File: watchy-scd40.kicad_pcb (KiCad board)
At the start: 2 copper layers, 10.3 x 17 mm, 12 parts, among them U1 SCD40-D-R2, U2 NJM2882F33

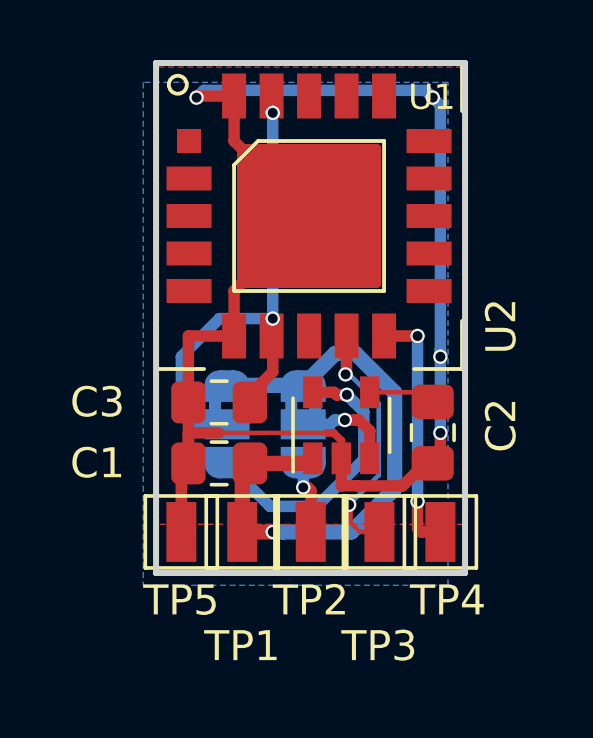
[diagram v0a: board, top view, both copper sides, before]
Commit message: v2: Tweaks to soldermask and to silkscreen
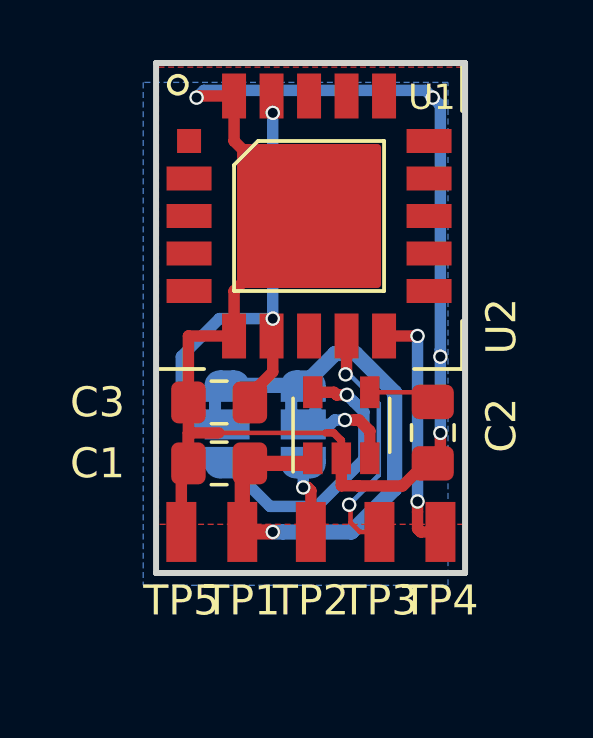
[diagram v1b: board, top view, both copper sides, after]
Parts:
- TP1, TP2, TP3, TP4, TP5: footprint TestPoint:TestPoint_Pad_2.0x2.0mm -> scd40:TestPoint_Pad_2.0x2.0mm-nosilk
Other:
- rule pad_to_mask_clearance: 0.051 -> 0.05
- rule solder_mask_min_width: 0.25 -> 0.2
- board text added: "ALWAYS ON"
- board text added: "CSA v2 20210823"
- board text added: "GPIO0"
- board text added: "REG"
- board text added: "UNREG"

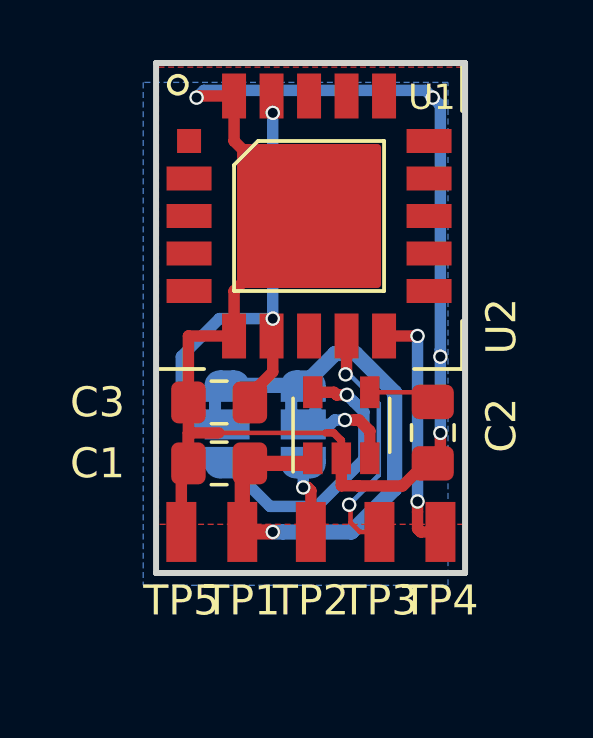
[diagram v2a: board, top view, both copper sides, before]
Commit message: Improve README; fix visibility of component labels on silkscreen layer
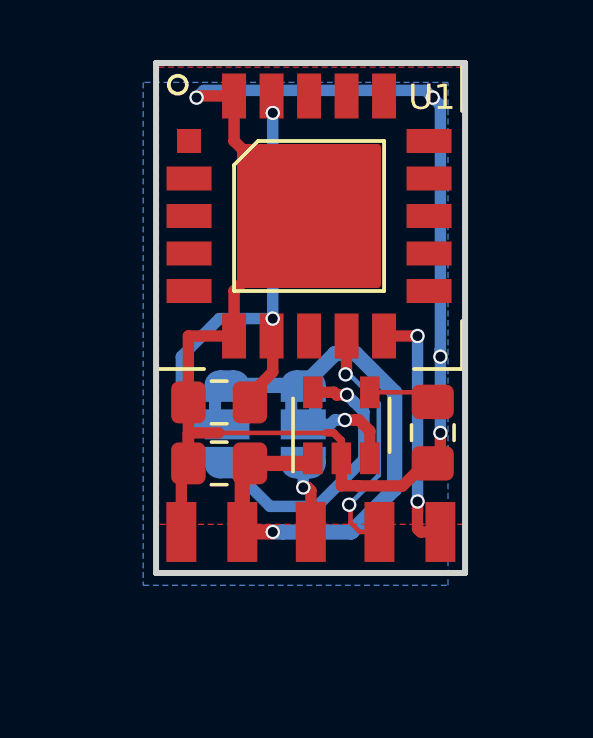
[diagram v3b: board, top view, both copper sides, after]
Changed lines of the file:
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@@
     (38 B.Mask user)
     (39 F.Mask user)
-    (40 Dwgs.User user)
-    (41 Cmts.User user)
-    (42 Eco1.User user)
-    (43 Eco2.User user)
+    (40 Dwgs.User user hide)
+    (41 Cmts.User user hide)
+    (42 Eco1.User user hide)
+    (43 Eco2.User user hide)
     (44 Edge.Cuts user)
-    (45 Margin user)
-    (46 B.CrtYd user)
-    (47 F.CrtYd user)
-    (48 B.Fab user)
-    (49 F.Fab user)
+    (45 Margin user hide)
+    (46 B.CrtYd user hide)
+    (47 F.CrtYd user hide)
+    (48 B.Fab user hide)
+    (49 F.Fab user hide)
   )
   (setup
@@
     (tags "test point SMD pad rectangle square")
     (attr virtual)
-    (fp_text reference TP5 (at 0 2.286) (layer F.SilkS)
+    (fp_text reference TP5 (at 0 2.286) (layer Cmts.User)
       (effects (font (size 1 1) (thickness 0.15)))
     )
@@
     (tags "test point SMD pad rectangle square")
     (attr virtual)
-    (fp_text reference TP4 (at 0 2.286) (layer F.SilkS)
+    (fp_text reference TP4 (at 0 2.286) (layer Cmts.User)
       (effects (font (size 1 1) (thickness 0.15)))
     )
@@
     (tags "test point SMD pad rectangle square")
     (attr virtual)
-    (fp_text reference TP3 (at 0 2.286) (layer F.SilkS)
+    (fp_text reference TP3 (at 0 2.286) (layer Cmts.User)
       (effects (font (size 1 1) (thickness 0.15)))
     )
@@
     (tags "test point SMD pad rectangle square")
     (attr virtual)
-    (fp_text reference TP2 (at 0 2.286) (layer F.SilkS)
+    (fp_text reference TP2 (at 0 2.286) (layer Cmts.User)
       (effects (font (size 1 1) (thickness 0.15)))
     )
@@
     (tags "test point SMD pad rectangle square")
     (attr virtual)
-    (fp_text reference TP1 (at 0 2.286) (layer F.SilkS)
+    (fp_text reference TP1 (at 0 2.286) (layer Cmts.User)
       (effects (font (size 1 1) (thickness 0.15)))
     )
@@
     (tags "capacitor handsolder")
     (attr smd)
-    (fp_text reference C3 (at 4.055 0 180) (layer F.SilkS)
+    (fp_text reference C3 (at 4.055 0 180) (layer Cmts.User)
       (effects (font (size 1 1) (thickness 0.15)))
     )
@@
     (tags "capacitor handsolder")
     (attr smd)
-    (fp_text reference C2 (at -0.245 -2.286 270) (layer F.SilkS)
+    (fp_text reference C2 (at -0.245 -2.286 270) (layer Cmts.User)
       (effects (font (size 1 1) (thickness 0.15)))
     )
@@
     (tags "capacitor handsolder")
     (attr smd)
-    (fp_text reference C1 (at 4.055 0 180) (layer F.SilkS)
+    (fp_text reference C1 (at 4.055 0 180) (layer Cmts.User)
       (effects (font (size 1 1) (thickness 0.15)))
     )
@@
     (tags "solder jumper open")
     (attr virtual)
-    (fp_text reference JP2 (at -0.224 -7.112) (layer B.SilkS)
-      (effects (font (size 1 1) (thickness 0.15)) (justify mirror))
+    (fp_text reference JP2 (at -0.224 -7.112) (layer Cmts.User)
+      (effects (font (size 1 1) (thickness 0.15)))
     )
     (fp_text value "EN SEL" (at 0 -1.9 270) (layer B.Fab)
@@
     (tags "solder jumper open")
     (attr virtual)
-    (fp_text reference JP1 (at 0.03 5.334) (layer B.SilkS)
-      (effects (font (size 1 1) (thickness 0.15)) (justify mirror))
+    (fp_text reference JP1 (at 0.03 5.334) (layer Cmts.User)
+      (effects (font (size 1 1) (thickness 0.15)))
     )
     (fp_text value "V SELECT" (at 0 -1.9 270) (layer B.Fab)
@@
     (tags SOT-23-5)
     (attr smd)
-    (fp_text reference U2 (at 3.302 5.334 90) (layer F.SilkS)
-      (effects (font (size 1 1) (thickness 0.15)))
-    )
+    (fp_text reference U2 (at 3.302 5.334 90) (layer Cmts.User)
+      (effects (font (size 1 1) (thickness 0.15)))
+    )
